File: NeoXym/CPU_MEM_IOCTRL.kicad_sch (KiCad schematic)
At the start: 23 parts, among them J10 Conn_01x28, J3 Conn_01x08, J4 Conn_01x08, J5 Conn_01x08, J6 Conn_01x08, J7 Conn_01x05, J8 Conn_01x05, U11 74HCT273, U12 W65C51N, U13 6502, U14 74HCT244, U16 74HC14, U20 WD65C22, U3 2764, U7 HM62256BLP, U9 74HCT00

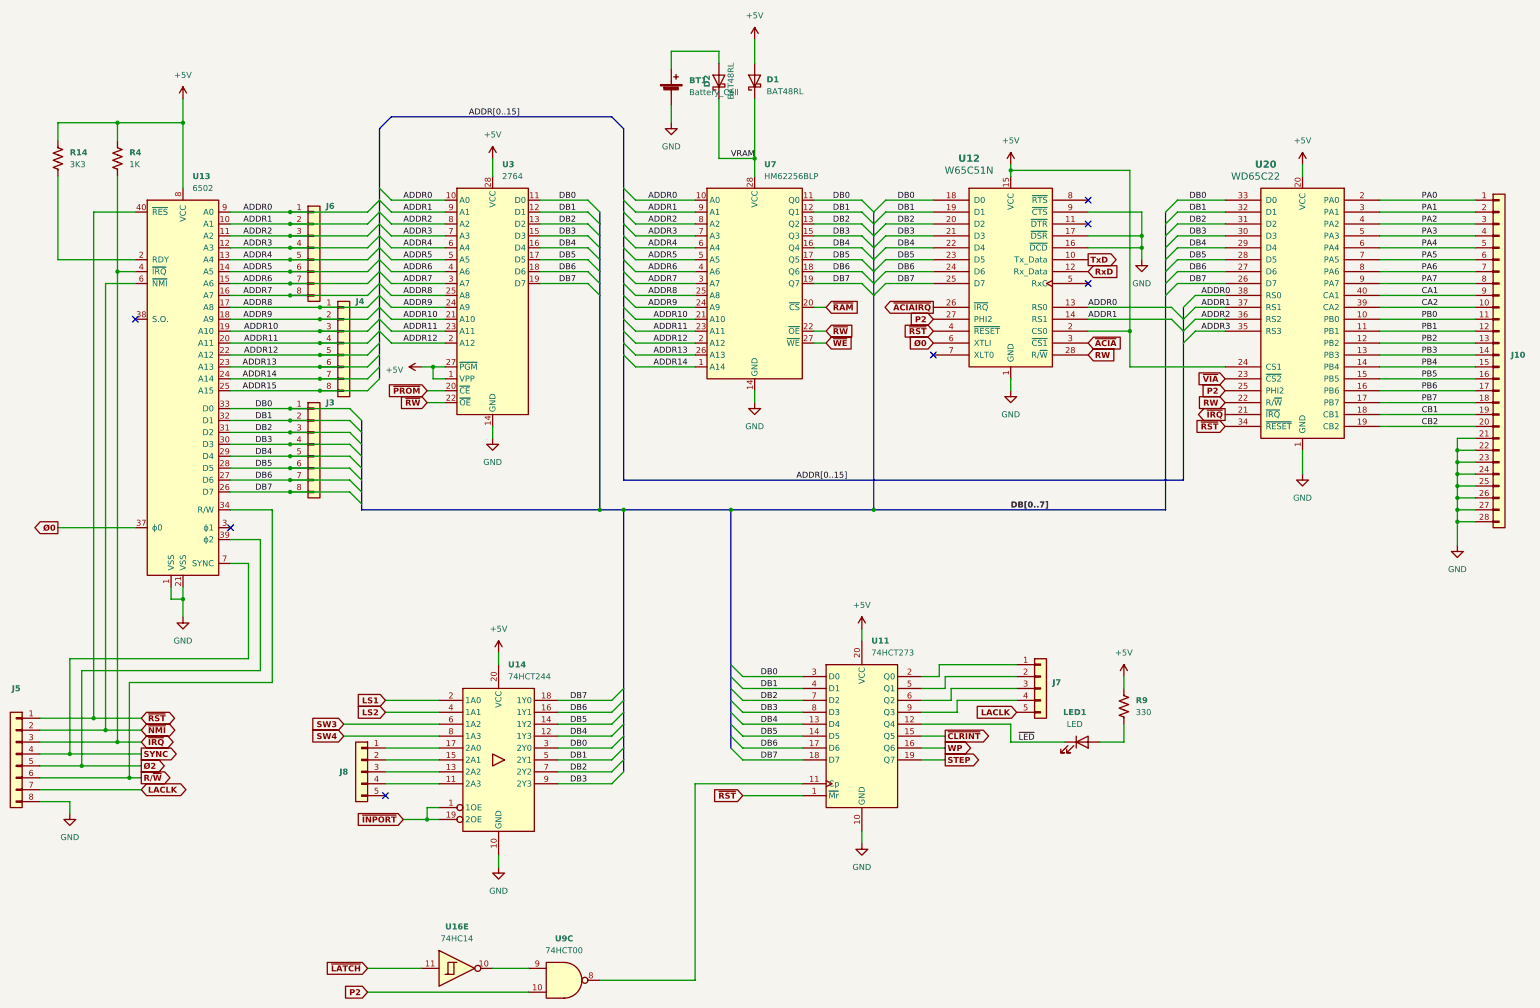
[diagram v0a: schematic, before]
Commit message: modified:   NeoXym/CPU_MEM_IOCTRL.kicad_sch 	modified:   NeoXym/XYMGLUE.kicad_sch 	modified:   NeoXym/XYMPOWER.kicad_sch
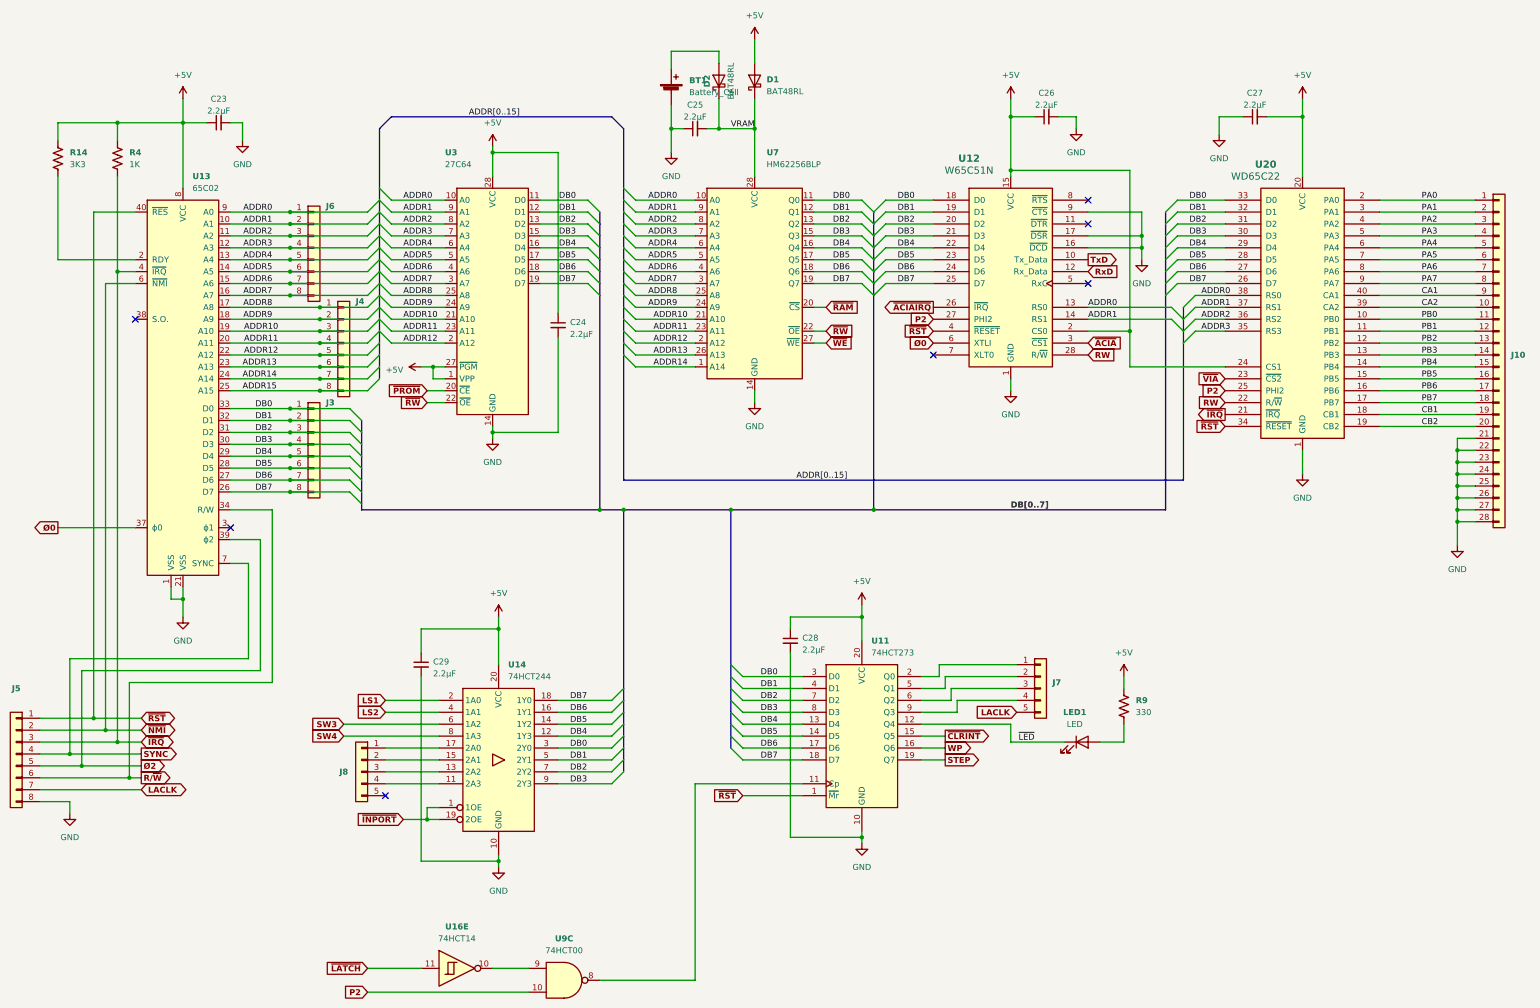
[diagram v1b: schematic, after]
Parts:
- added C23, C24, C25, C26, C27, C28, C29: 2.2µF, symbol Device:C_Small
- U13: value 6502 -> 65C02
- U16: value 74HC14 -> 74HCT14
- U3: value 2764 -> 27C64
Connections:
- net +5V: now also C23.1, C24.1, C26.1, C27.2, C28.1, C29.1
- net GND: now also C23.2, C24.2, C25.1, C26.2, C27.1, C28.2, C29.2
- net VRAM: now also C25.2

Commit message: modified:   CPU_MEM_IOCTRL.kicad_sch 	modified:   XYMGLUE.kicad_sch 	modified:   XYMPOWER.kicad_sch
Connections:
- net ~{ACIA} renamed ~{ACIA0}
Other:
- note added: "DCE (DEBUG/XYM) UART"
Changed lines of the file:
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@@
   (junction (at 81.28 187.96) (diameter 0) (color 0 0 0 0)
   )
-  (junction (at 294.64 92.71) (diameter 0) (color 0 0 0 0)
-  )
   (junction (at 121.92 90.17) (diameter 0) (color 0 0 0 0)
   )
@@
   (junction (at 115.57 127) (diameter 0) (color 0 0 0 0)
   )
+  (junction (at 313.69 100.33) (diameter 0) (color 0 0 0 0)
+  )
   (junction (at 115.57 80.01) (diameter 0) (color 0 0 0 0)
   )
@@
   (junction (at 158.75 114.3) (diameter 0) (color 0 0 0 0)
   )
-  (junction (at 269.24 58.42) (diameter 0) (color 0 0 0 0)
-  )
   (junction (at 78.74 180.34) (diameter 0) (color 0 0 0 0)
   )
@@
     (stroke (width 0) (type default))
   )
-  (wire (pts (xy 285.75 92.71) (xy 294.64 92.71))
-    (stroke (width 0) (type default))
-  )
   (wire (pts (xy 347.98 64.77) (xy 368.3 64.77))
     (stroke (width 0) (type default))
@@
     (stroke (width 0) (type default))
   )
+  (wire (pts (xy 313.69 100.33) (xy 314.96 100.33))
+    (stroke (width 0) (type default))
+  )
   (wire (pts (xy 68.58 195.58) (xy 68.58 193.04))
     (stroke (width 0) (type default))
@@
     (stroke (width 0) (type default))
   )
+  (wire (pts (xy 297.18 92.71) (xy 297.18 100.33))
+    (stroke (width 0) (type default))
+  )
   (bus (pts (xy 186.69 62.23) (xy 186.69 64.77))
     (stroke (width 0) (type default))
@@
     (stroke (width 0) (type default))
   )
-  (wire (pts (xy 294.64 58.42) (xy 269.24 58.42))
-    (stroke (width 0) (type default))
-  )
   (wire (pts (xy 285.75 87.63) (xy 303.53 87.63))
     (stroke (width 0) (type default))
@@
     (stroke (width 0) (type default))
   )
+  (wire (pts (xy 285.75 92.71) (xy 297.18 92.71))
+    (stroke (width 0) (type default))
+  )
   (wire (pts (xy 254 166.37) (xy 250.19 166.37))
     (stroke (width 0) (type default))
@@
     (stroke (width 0) (type default))
   )
-  (wire (pts (xy 269.24 46.99) (xy 269.24 58.42))
-    (stroke (width 0) (type default))
-  )
   (bus (pts (xy 186.69 72.39) (xy 186.69 74.93))
     (stroke (width 0) (type default))
@@
     (stroke (width 0) (type default))
   )
-  (wire (pts (xy 314.96 100.33) (xy 294.64 100.33))
-    (stroke (width 0) (type default))
-  )
   (wire (pts (xy 115.57 116.84) (xy 102.87 116.84))
     (stroke (width 0) (type default))
@@
     (stroke (width 0) (type default))
   )
-  (wire (pts (xy 294.64 100.33) (xy 294.64 92.71))
-    (stroke (width 0) (type default))
-  )
   (bus (pts (xy 134.62 49.53) (xy 134.62 62.23))
     (stroke (width 0) (type default))
@@
     (stroke (width 0) (type default))
   )
+  (wire (pts (xy 313.69 99.06) (xy 313.69 100.33))
+    (stroke (width 0) (type default))
+  )
   (wire (pts (xy 92.71 48.26) (xy 92.71 62.23))
     (stroke (width 0) (type default))
@@
     (stroke (width 0) (type default))
   )
+  (wire (pts (xy 297.18 100.33) (xy 313.69 100.33))
+    (stroke (width 0) (type default))
+  )
   (wire (pts (xy 255.27 184.15) (xy 250.19 184.15))
     (stroke (width 0) (type default))
@@
     (stroke (width 0) (type default))
   )
-  (wire (pts (xy 294.64 92.71) (xy 294.64 58.42))
-    (stroke (width 0) (type default))
-  )
-  (wire (pts (xy 269.24 58.42) (xy 269.24 59.69))
+  (wire (pts (xy 269.24 46.99) (xy 269.24 59.69))
     (stroke (width 0) (type default))
   )
@@
     (stroke (width 0) (type default))
   )
+  (text "DCE (DEBUG/XYM) UART" (at 250.19 118.11 0)
+    (effects (font (size 2.54 2.54) bold) (justify left bottom))
+  )
   (label "DB0" (at 111.76 109.22 180) (fields_autoplaced)
     (effects (font (size 1.27 1.27)) (justify right bottom))
@@
     )
   )
-  (global_label "Ø0" (shape output) (at 66.04 134.62 180) (fields_autoplaced)
+  (global_label "Ø0" (shape input) (at 66.04 134.62 180) (fields_autoplaced)
     (effects (font (face "Consolas") (size 1.27 1.27) bold) (justify right))
-    (property "Intersheetrefs" "${INTERSHEET_REFS}" (at 61.7521 134.62 0)
+    (property "Intersheetrefs" "${INTERSHEET_REFS}" (at 61.1339 134.62 0)
       (effects (font (size 1.27 1.27)) (justify right) hide)
     )
@@
     )
   )
-  (global_label "~{ACIA}" (shape input) (at 285.75 95.25 0) (fields_autoplaced)
+  (global_label "~{ACIA0}" (shape input) (at 285.75 95.25 0) (fields_autoplaced)
     (effects (font (face "Consolas") (size 1.27 1.27) bold) (justify left))
-    (property "Intersheetrefs" "${INTERSHEET_REFS}" (at 292.4806 95.25 0)
+    (property "Intersheetrefs" "${INTERSHEET_REFS}" (at 293.6649 95.25 0)
       (effects (font (size 1.27 1.27)) (justify left) hide)
     )
@@
         )
       )
+    )
+  )
+  (symbol (lib_id "power:+5V") (at 313.69 99.06 0) (unit 1)
+    (in_bom yes) (on_board yes) (dnp no)
+    (property "Reference" "#PWR02" (at 313.69 102.87 0)
+      (effects (font (size 1.27 1.27) bold) hide)
+    )
+    (property "Value" "+5V" (at 313.69 95.25 0)
+      (effects (font (size 1.27 1.27)))
+    )
+    (property "Footprint" "" (at 313.69 99.06 0)
+      (effects (font (size 1.27 1.27)) hide)
+    )
+    (property "Datasheet" "" (at 313.69 99.06 0)
+      (effects (font (size 1.27 1.27)) hide)
+    )
+    (pin "1")
+    (instances
+      (project "NeoXym"
+        (path "/e63e39d7-6ac0-4ffd-8aa3-1841a4541b55"
+          (reference "#PWR02") (unit 1)
+        )
+        (path "/e63e39d7-6ac0-4ffd-8aa3-1841a4541b55/148f0f12-bed5-4ea7-9fc2-19a7c5d7f7be"
+          (reference "#PWR065") (unit 1)
+        )
+      )
